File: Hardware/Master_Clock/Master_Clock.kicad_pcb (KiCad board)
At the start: 2 copper layers, 42 parts, among them J1 Phoenix Contact 1935161, J2 Phoenix Contact 1935161, J3 Conn_01x03_Pin, Q1 BC847, SW1 SW_Push, SW2 SW_Push, U1 LT1178S8, U2 LT8330, U3 OP193FS, U4 AP7370-18W5, U5 ATtiny402-SS, X1 SG-3031CM

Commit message: HW V1.0.
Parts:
- removed the TP1 at (155.9, 100.8)
- added H1: MountingHole, MountingHole:MountingHole_3.2mm_M3_ISO7380_Pad, F.Cu at (147.0, 61.5)
- added H2: MountingHole, MountingHole:MountingHole_3.2mm_M3_ISO7380_Pad, F.Cu at (161.0, 106.5)
- added R11: 0R, Resistor_SMD:R_0603_1608Metric_Pad0.98x0.95mm_HandSolder, B.Cu at (145.5, 113.5)
- added R12: 0R, Resistor_SMD:R_0603_1608Metric_Pad0.98x0.95mm_HandSolder, B.Cu at (149.0, 97.5)
- C1, C10, C11, C12, C13, C14, C2, C3, C6, C7, C8, C9, D1, L1, Q1, R1, R10, R2, R3, R4, R5, R6, R7, R8, R9, TP2, U1, U2, U3, U4, U5, X1: moved to B.Cu
- TP1: renamed from TP3; moved to B.Cu
- moved U4 55.8 mm to (156.0, 68.5), turned to 180 degrees
- moved X1 52.9 mm to (148.0, 72.0), turned to 180 degrees
- moved C13 43.7 mm to (148.0, 74.5), turned to 180 degrees
- moved C11 41.9 mm to (156.0, 75.5)
- moved L1 40.9 mm to (160.5, 99.5), turned to -90 degrees
- moved R6 40.0 mm to (148.0, 77.0), turned to 180 degrees
- moved U2 35.5 mm to (153.5, 100.0), turned to 90 degrees
- moved J2 33.8 mm to (155.0, 120.0)
- moved U1 33.6 mm to (150.0, 113.8), turned to 90 degrees
- moved C4 33.5 mm to (145.5, 107.3), turned to 90 degrees
- moved C10 33.1 mm to (148.0, 78.5)
- moved C14 32.8 mm to (148.0, 69.5), turned to 180 degrees
- moved C12 32.5 mm to (156.0, 90.0)
- moved J1 32.0 mm to (160.0, 63.0), turned to 180 degrees
- moved D1 31.7 mm to (157.0, 103.0), turned to 90 degrees
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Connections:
- C11 pad 1: /Key2 -> /Key1
- C12 pad 1: /Key1 -> /Key2
- D2 pad 2: Net-(D2-A) -> +BATT
- Q1 pad 3: Net-(D2-K) -> Net-(Q1-C)
- R5 pad 1: +BATT -> Net-(D2-K)
- R5 pad 2: Net-(D2-A) -> Net-(Q1-C)
- R7 pad 2: /Key2 -> /Key1
- R8 pad 2: /Key1 -> /Key2
- SW1 pad 1: /Key2 -> /Key1
- SW2 pad 1: /Key1 -> /Key2
- U1 pad 7: Net-(C5-Pad1) -> Net-(R11-Pad1)
- U2 pad 4: +BATT -> Net-(U2-EN/UVLO)
- U3 pad 6: Net-(C5-Pad1) -> Net-(R11-Pad1)
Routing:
- net GND: track 0.00 -> 235.8 mm, vias 0 -> 23
- net +1V8: track 0.00 -> 111.9 mm, vias 0 -> 4
- net +BATT: track 0.00 -> 71.5 mm, vias 0 -> 1
- net /MinPulse: track 0.00 -> 49.4 mm, vias 0 -> 2
- net +24V: track 0.00 -> 29.0 mm
- net /Key1: track 0.00 -> 25.6 mm, vias 0 -> 1
- net /~{RESET}/UPDI: track 0.00 -> 20.0 mm
- net /Key2: track 0.00 -> 17.5 mm
- net Net-(U1A--): track 0.00 -> 15.9 mm
- net Net-(R11-Pad1): track 0.00 -> 15.7 mm
- net /32kHz: track 0.00 -> 14.8 mm
- net /SlaveClock: track 0.00 -> 10.1 mm
- net /LED: track 0.00 -> 8.69 mm
- net Net-(U2-FBX): track 0.00 -> 6.40 mm
- net Net-(D1-A): track 0.00 -> 6.06 mm
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- added copper zone on F.Cu, net GND
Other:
- board outline added: 20 x 67 mm
- board text added: "3..10V"
- board text added: "Clock"
- board text added: "GND UPDI 1V8"
- board text added: "Master Clock V1.0 12/2023 C. Mauderer"
- board text added: "PAUSE"
- board text added: "STEP"
- board text added: "c-mauderer.de/s/master-clock"

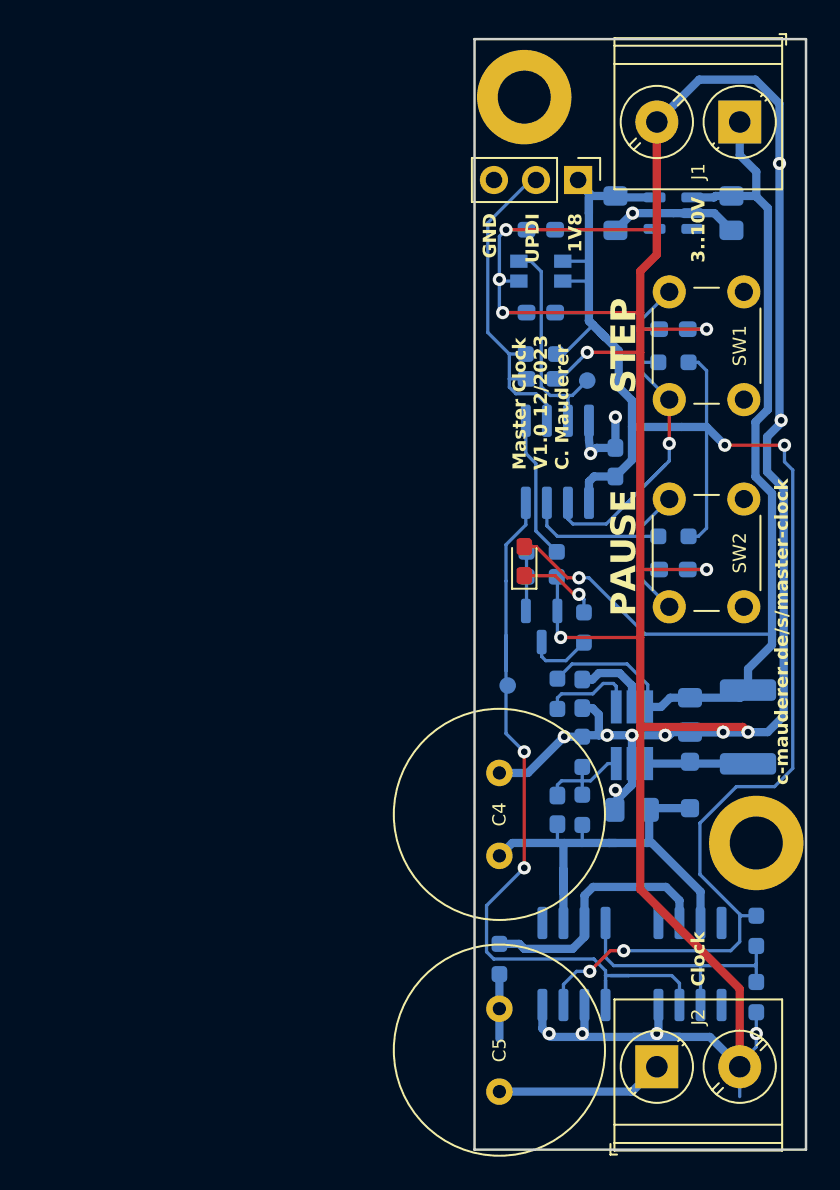
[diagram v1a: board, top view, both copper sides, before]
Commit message: HW V1.0-2023-12-28 - Add 0R-resistors in supply.
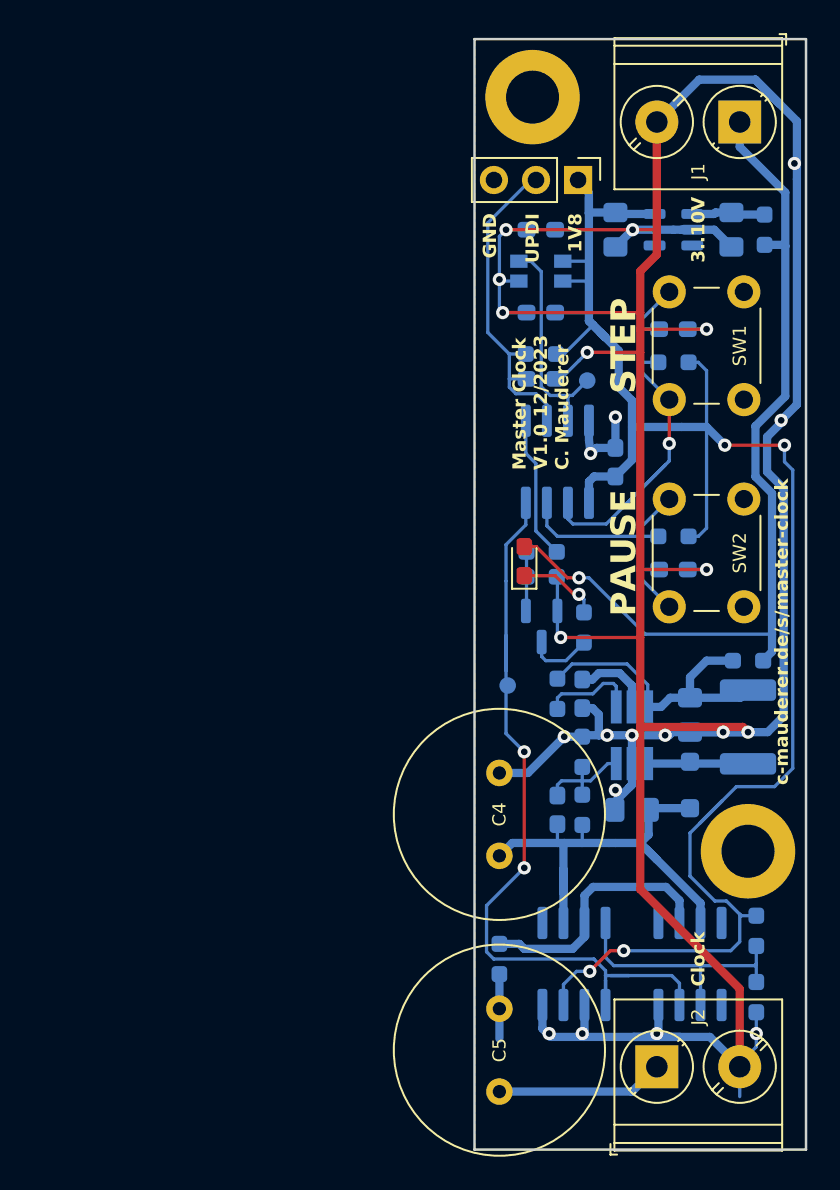
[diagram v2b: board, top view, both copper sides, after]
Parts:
- added R13: 0R, Resistor_SMD:R_0603_1608Metric_Pad0.98x0.95mm_HandSolder, B.Cu at (160.5, 95.5)
- added R14: 0R, Resistor_SMD:R_0603_1608Metric_Pad0.98x0.95mm_HandSolder, B.Cu at (161.5, 69.5)
- moved C8 1.00 mm to (159.5, 69.5)
- moved C9 1.00 mm to (152.5, 69.5)
- moved U4 1.00 mm to (156.0, 69.5)
- moved H2 0.71 mm to (160.5, 107.0)
- moved H1 0.50 mm to (147.5, 61.5)
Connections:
- C2 pad 1: +BATT -> Net-(U2-Vin)
- C8 pad 1: +BATT -> Net-(U4-VI)
- L1 pad 1: +BATT -> Net-(U2-Vin)
- R12 pad 2: +BATT -> Net-(U2-Vin)
- U2 pad 6: +BATT -> Net-(U2-Vin)
- U4 pad 1: +BATT -> Net-(U4-VI)
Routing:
- net Net-(U2-Vin): track 0.00 -> 18.4 mm
- net +BATT: track 71.5 -> 53.4 mm
- net Net-(U4-VI): track 0.00 -> 4.45 mm
- net GND: track 235.8 -> 238.6 mm
- net +1V8: track 111.9 -> 113.5 mm
